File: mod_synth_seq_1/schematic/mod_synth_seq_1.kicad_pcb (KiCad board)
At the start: 2 copper layers, 38.1 x 109.2 mm, 43 parts, among them J1 CV1, J10 Reset, J11 Clock, J12 Gate Out, J2 Step 1 Gate, J3 Step 2 Gate, J4 Step 3 Gate, J5 Step 4 Gate

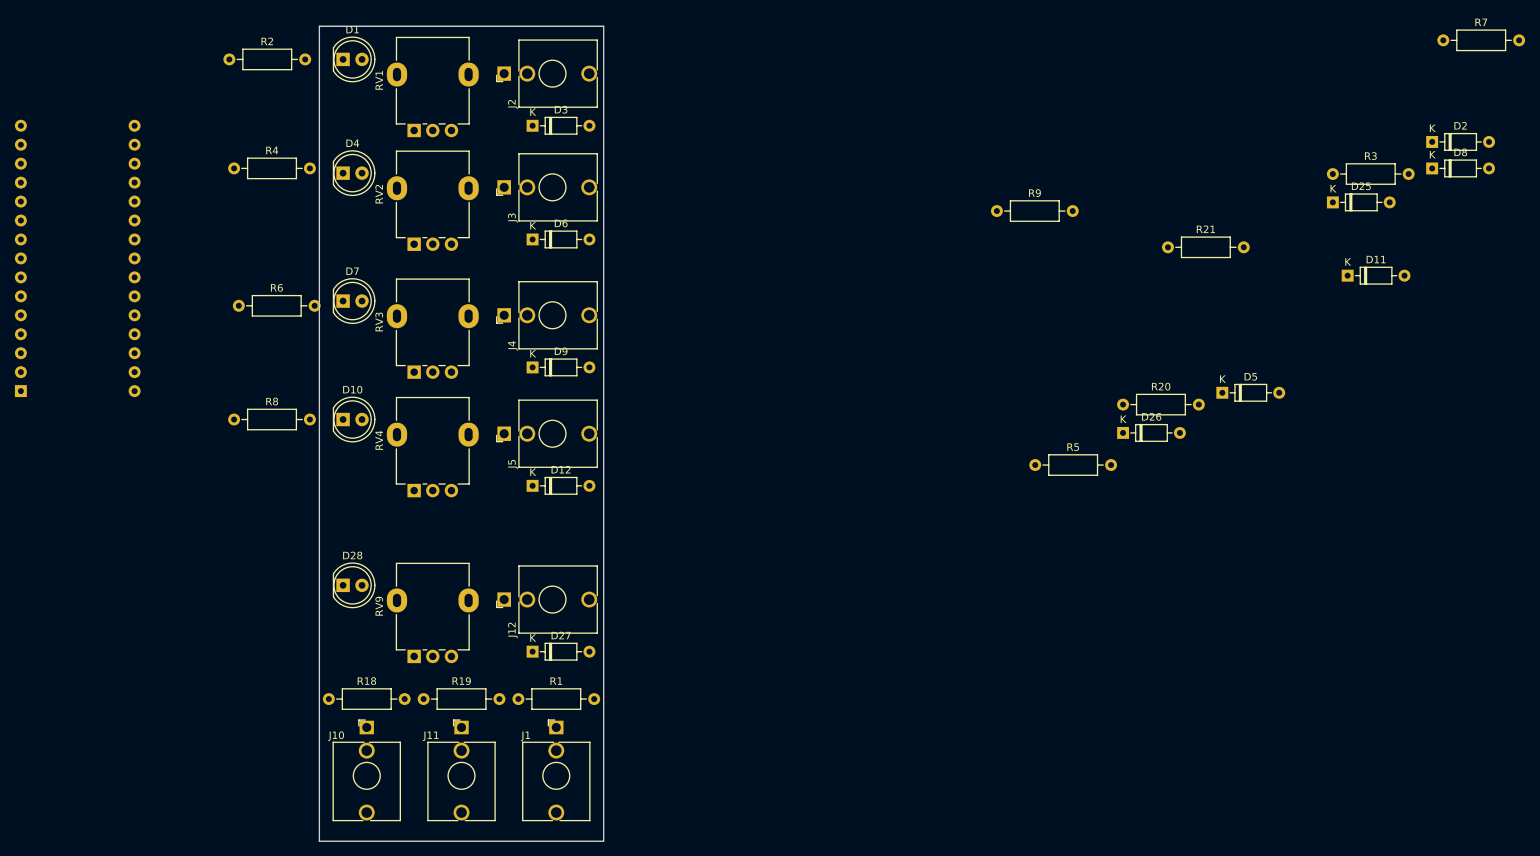
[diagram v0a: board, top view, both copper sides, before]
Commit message: Add missing connector
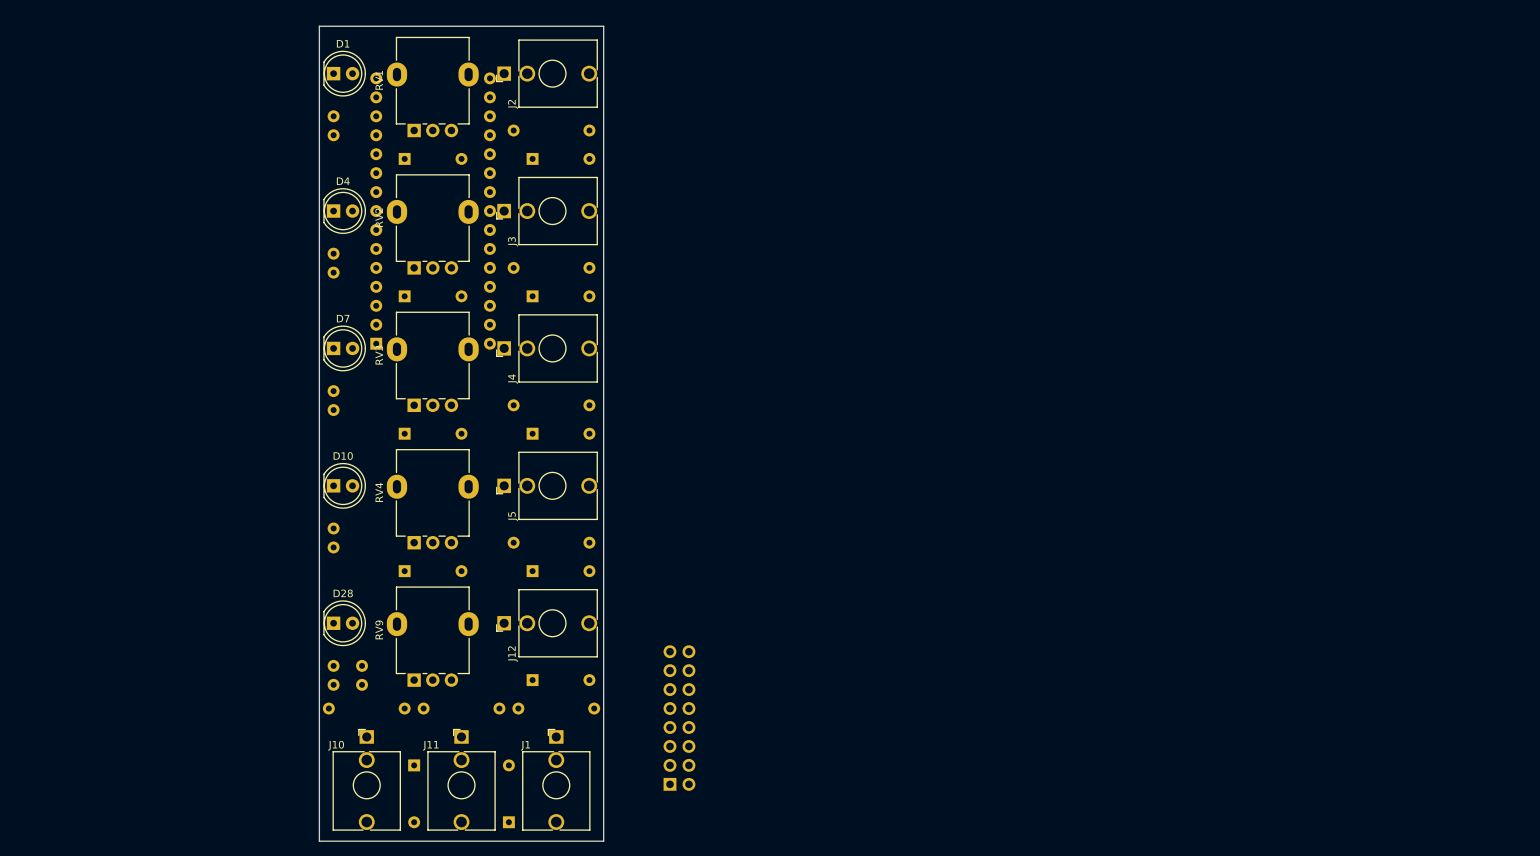
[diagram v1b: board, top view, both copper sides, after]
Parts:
- added J6: Conn_02x08_Odd_Even, Connector_IDC:IDC-Header_2x08_P2.54mm_Vertical, B.Cu at (110.5, 120.7)
- D11, D12, D2, D25, D26, D27, D3, D5, D6, D8, D9, R1, R18, R19, R3, R5, R7, R9: moved to B.Cu
- R2, R20, R21, R4, R6, R8: footprint Resistor_THT:R_Axial_DIN0207_L6.3mm_D2.5mm_P10.16mm_Horizontal -> Resistor_THT:R_Axial_DIN0207_L6.3mm_D2.5mm_P2.54mm_Vertical; moved to B.Cu
- moved D25 144.4 mm to (76.2, 118.1), turned to 270 degrees
- moved D8 142.2 mm to (74.9, 73.7)
- moved D2 137.7 mm to (74.9, 36.8)
- moved R7 133.9 mm to (89.5, 69.8)
- moved D11 132.4 mm to (74.9, 92.1)
- moved R21 125.1 mm to (65.4, 104.8), turned to 270 degrees
- moved D5 110.4 mm to (74.9, 55.2)
- moved R3 109.9 mm to (89.5, 33.0)
- moved R20 107.8 mm to (69.2, 104.8), turned to 270 degrees
- moved D26 97.5 mm to (88.9, 125.7), turned to 90 degrees
- moved R9 78.6 mm to (89.5, 88.3)
- moved R5 74.7 mm to (89.5, 51.4)
- moved A1 48.0 mm to (71.1, 61.6)
- moved R8 19.8 mm to (65.4, 86.4), turned to 270 degrees
- moved R4 17.6 mm to (65.4, 49.5), turned to 270 degrees
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
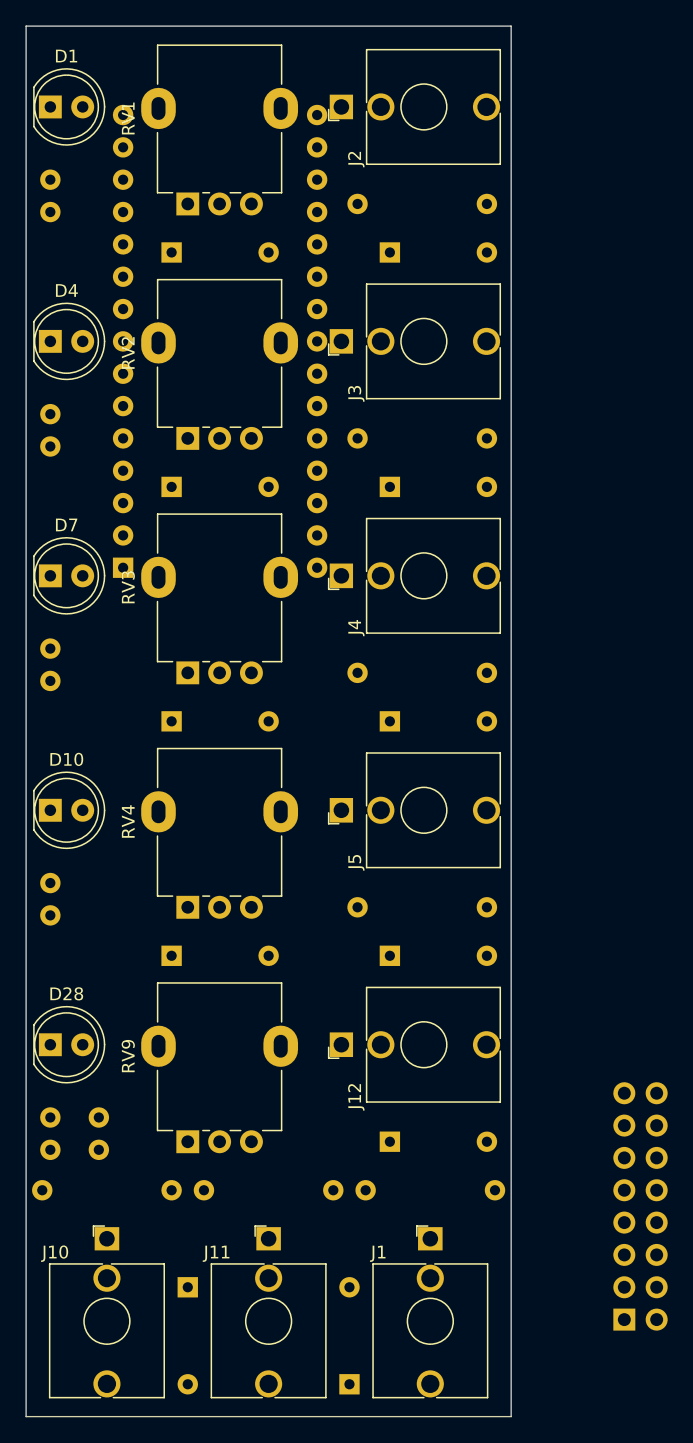
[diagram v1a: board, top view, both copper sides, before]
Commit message: Remove gate from smaller sequencer
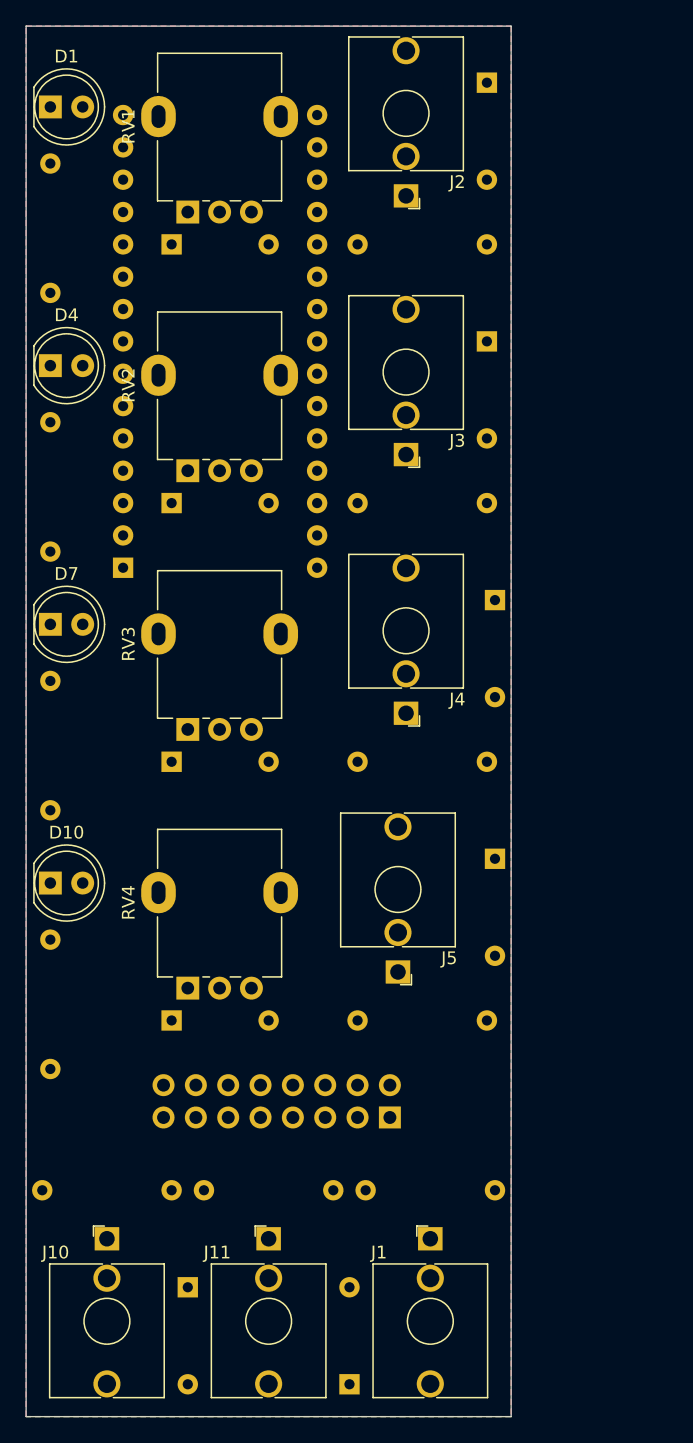
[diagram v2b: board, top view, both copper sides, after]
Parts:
- removed D27: 1N4148, Diode_THT:D_DO-35_SOD27_P7.62mm_Horizontal
- removed D28: LED, LED_THT:LED_D5.0mm
- removed J12: Gate Out, Connector_Audio:Jack_3.5mm_QingPu_WQP-PJ398SM_Vertical_CircularHoles
- removed R20, R21: 1k, Resistor_THT:R_Axial_DIN0207_L6.3mm_D2.5mm_P2.54mm_Vertical
- removed RV9: 100k Lin, Potentiometer_THT:Potentiometer_Alpha_RD901F-40-00D_Single_Vertical
- R2, R4, R6, R8: footprint Resistor_THT:R_Axial_DIN0207_L6.3mm_D2.5mm_P2.54mm_Vertical -> Resistor_THT:R_Axial_DIN0207_L6.3mm_D2.5mm_P10.16mm_Horizontal
- moved J6 24.3 mm to (92.1, 104.8), turned to 90 degrees
- moved D3 15.4 mm to (99.7, 23.5), turned to 270 degrees
- moved D6 13.7 mm to (99.7, 43.8), turned to 270 degrees
- moved J5 13.5 mm to (92.7, 93.3), turned to 180 degrees
- moved D9 12.6 mm to (100.3, 64.1), turned to 270 degrees
- moved J4 11.9 mm to (93.3, 73.0), turned to 180 degrees
- moved D12 11.2 mm to (100.3, 84.5), turned to 270 degrees
- moved J3 10.2 mm to (93.3, 52.7), turned to 180 degrees
- moved R9 8.89 mm to (89.5, 97.2)
- moved J2 8.64 mm to (93.3, 32.4), turned to 180 degrees
- moved R7 6.98 mm to (89.5, 76.8)
- moved RV4 6.35 mm to (76.2, 94.6)
- moved D10 5.72 mm to (65.4, 86.4)
- moved D11 5.08 mm to (74.9, 97.2)
- moved R5 5.08 mm to (89.5, 56.5)
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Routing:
- added copper zone on B.Cu, net GND
- added copper zone on F.Cu, net GND

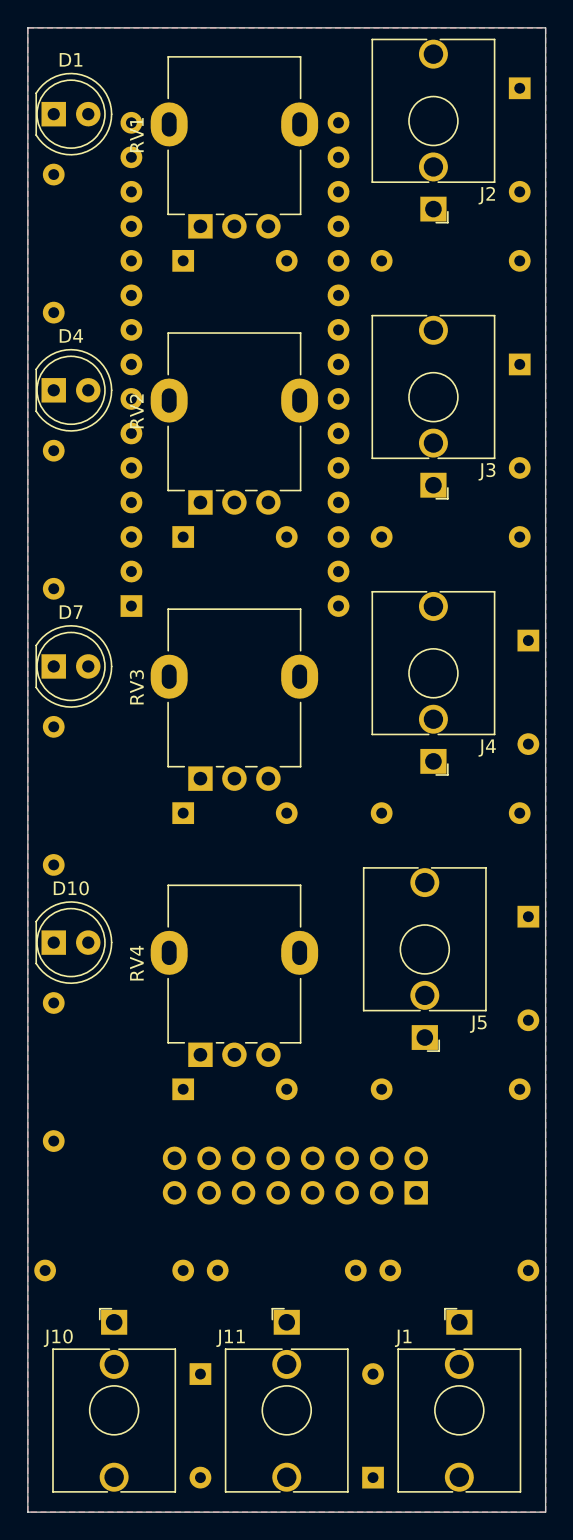
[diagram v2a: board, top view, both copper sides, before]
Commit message: Layout PCB for seq_1
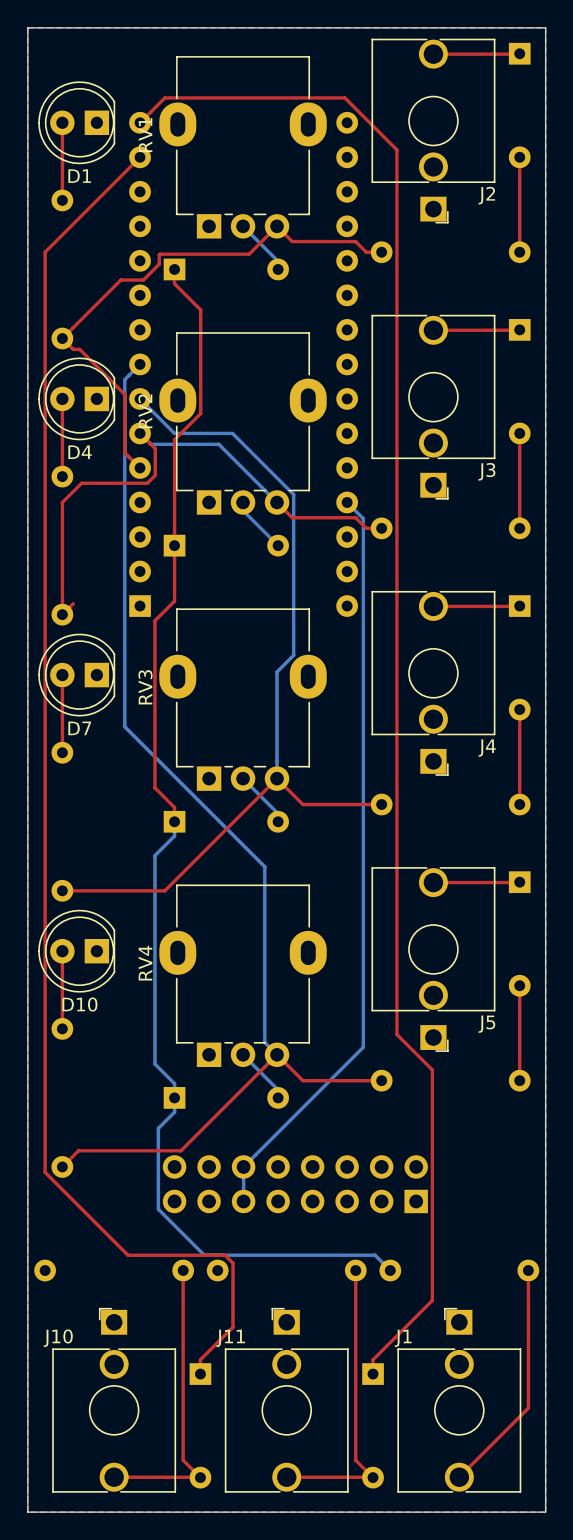
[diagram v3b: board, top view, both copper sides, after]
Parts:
- moved D26 7.62 mm to (88.9, 118.1), turned to 270 degrees
- moved D10 3.24 mm to (68.6, 87.0), turned to 180 degrees
- moved D1 3.24 mm to (68.6, 26.0), turned to 180 degrees
- moved D4 3.24 mm to (68.6, 46.4), turned to 180 degrees
- moved D7 3.24 mm to (68.6, 66.7), turned to 180 degrees
- moved D9 2.62 mm to (99.7, 61.6)
- moved D12 2.62 mm to (99.7, 81.9)
- moved D3 2.54 mm to (99.7, 21.0)
- moved D6 2.54 mm to (99.7, 41.3)
- moved R2 2.01 mm to (66.0, 31.8)
- moved R4 2.01 mm to (66.0, 52.1)
- moved R6 2.01 mm to (66.0, 72.4)
- moved R8 2.01 mm to (66.0, 92.7)
- moved D11 0.90 mm to (74.3, 97.8)
- moved D8 0.90 mm to (74.3, 77.5)
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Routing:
- net Net-(A1-Pad15): track 0.00 -> 114.2 mm
- net Net-(A1-Pad14): track 0.00 -> 103.3 mm
- net Net-(D11-Pad1): track 0.00 -> 92.6 mm
- net Net-(A1-Pad8): track 0.00 -> 83.0 mm
- net Net-(A1-Pad7): track 0.00 -> 63.3 mm
- net +5V: track 0.00 -> 55.6 mm
- net Net-(A1-Pad6): track 0.00 -> 41.3 mm
- net Net-(A1-Pad5): track 0.00 -> 40.3 mm
- net Net-(D26-Pad2): track 0.00 -> 22.1 mm
- net Net-(D25-Pad2): track 0.00 -> 22.1 mm
- net Net-(J1-PadT): track 0.00 -> 17.3 mm
- net Net-(D3-Pad2): track 0.00 -> 6.99 mm
- net Net-(D9-Pad2): track 0.00 -> 6.98 mm
- net Net-(D6-Pad2): track 0.00 -> 6.98 mm
- net Net-(D12-Pad2): track 0.00 -> 6.98 mm
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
